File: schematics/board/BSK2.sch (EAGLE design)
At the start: 18 parts

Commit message: Реструктурированы сигналы коммутации для плат БСК
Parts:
- renumbered VAR1 to BSK1
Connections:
- net KEM1 renamed B2_KEM+
- net KEM2 renamed B2_KEM-
- net KHEAT1 renamed B2_KHEAT
- net KVCC1 renamed B2_KVCC
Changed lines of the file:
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@@
 <part name="U$11" library="CanCubeSat" deviceset="KCONNECT" device=""/>
 <part name="U$12" library="CanCubeSat" deviceset="KCONNECT" device=""/>
-<part name="VAR1" library="pinheadCS" deviceset="PINHD-1X8" device=""/>
+<part name="BSK1" library="pinheadCS" deviceset="PINHD-1X8" device=""/>
 </parts>
 <sheets>
@@
 <attribute name="NAME" x="140.462" y="102.362" size="1.27" layer="95"/>
 </instance>
-<instance part="VAR1" gate="A" x="154.94" y="175.26" smashed="yes" rot="R270">
+<instance part="BSK1" gate="A" x="154.94" y="175.26" smashed="yes" rot="R270">
 <attribute name="NAME" x="168.275" y="181.61" size="1.778" layer="95" rot="R270"/>
 <attribute name="VALUE" x="142.24" y="181.61" size="1.778" layer="96" rot="R270"/>
@@
 <wire x1="165.1" y1="177.8" x2="165.1" y2="190.5" width="0.1524" layer="91"/>
 <label x="165.1" y="182.88" size="1.778" layer="95" rot="R90"/>
-<pinref part="VAR1" gate="A" pin="1"/>
+<pinref part="BSK1" gate="A" pin="1"/>
 </segment>
 </net>
@@
 <wire x1="149.86" y1="177.8" x2="149.86" y2="190.5" width="0.1524" layer="91"/>
 <label x="149.86" y="182.88" size="1.778" layer="95" rot="R90"/>
-<pinref part="VAR1" gate="A" pin="7"/>
+<pinref part="BSK1" gate="A" pin="7"/>
 </segment>
 <segment>
@@
 <wire x1="152.4" y1="177.8" x2="152.4" y2="190.5" width="0.1524" layer="91"/>
 <label x="152.4" y="182.88" size="1.778" layer="95" rot="R90"/>
-<pinref part="VAR1" gate="A" pin="6"/>
+<pinref part="BSK1" gate="A" pin="6"/>
 </segment>
 </net>
-<net name="KEM1" class="0">
+<net name="B2_KEM+" class="0">
 <segment>
 <wire x1="160.02" y1="177.8" x2="160.02" y2="190.5" width="0.1524" layer="91"/>
 <label x="160.02" y="182.88" size="1.778" layer="95" rot="R90"/>
-<pinref part="VAR1" gate="A" pin="3"/>
+<pinref part="BSK1" gate="A" pin="3"/>
 </segment>
 <segment>
@@
 </segment>
 </net>
-<net name="KEM2" class="0">
+<net name="B2_KEM-" class="0">
 <segment>
 <wire x1="162.56" y1="177.8" x2="162.56" y2="190.5" width="0.1524" layer="91"/>
 <label x="162.56" y="182.88" size="1.778" layer="95" rot="R90"/>
-<pinref part="VAR1" gate="A" pin="2"/>
+<pinref part="BSK1" gate="A" pin="2"/>
 </segment>
 <segment>
@@
 </segment>
 </net>
-<net name="KHEAT1" class="0">
+<net name="B2_KHEAT" class="0">
 <segment>
 <wire x1="157.48" y1="177.8" x2="157.48" y2="190.5" width="0.1524" layer="91"/>
 <label x="157.48" y="182.88" size="1.778" layer="95" rot="R90"/>
-<pinref part="VAR1" gate="A" pin="4"/>
+<pinref part="BSK1" gate="A" pin="4"/>
 </segment>
 <segment>
@@
 </segment>
 </net>
-<net name="KVCC1" class="0">
+<net name="B2_KVCC" class="0">
 <segment>
 <wire x1="154.94" y1="177.8" x2="154.94" y2="190.5" width="0.1524" layer="91"/>
 <label x="154.94" y="182.88" size="1.778" layer="95" rot="R90"/>
-<pinref part="VAR1" gate="A" pin="5"/>
+<pinref part="BSK1" gate="A" pin="5"/>
 </segment>
 <segment>
@@
 <wire x1="147.32" y1="177.8" x2="147.32" y2="190.5" width="0.1524" layer="91"/>
 <label x="147.32" y="182.88" size="1.778" layer="95" rot="R90"/>
-<pinref part="VAR1" gate="A" pin="8"/>
-</segment>
-<segment>
+<pinref part="BSK1" gate="A" pin="8"/>
+</segment>
+<segment>

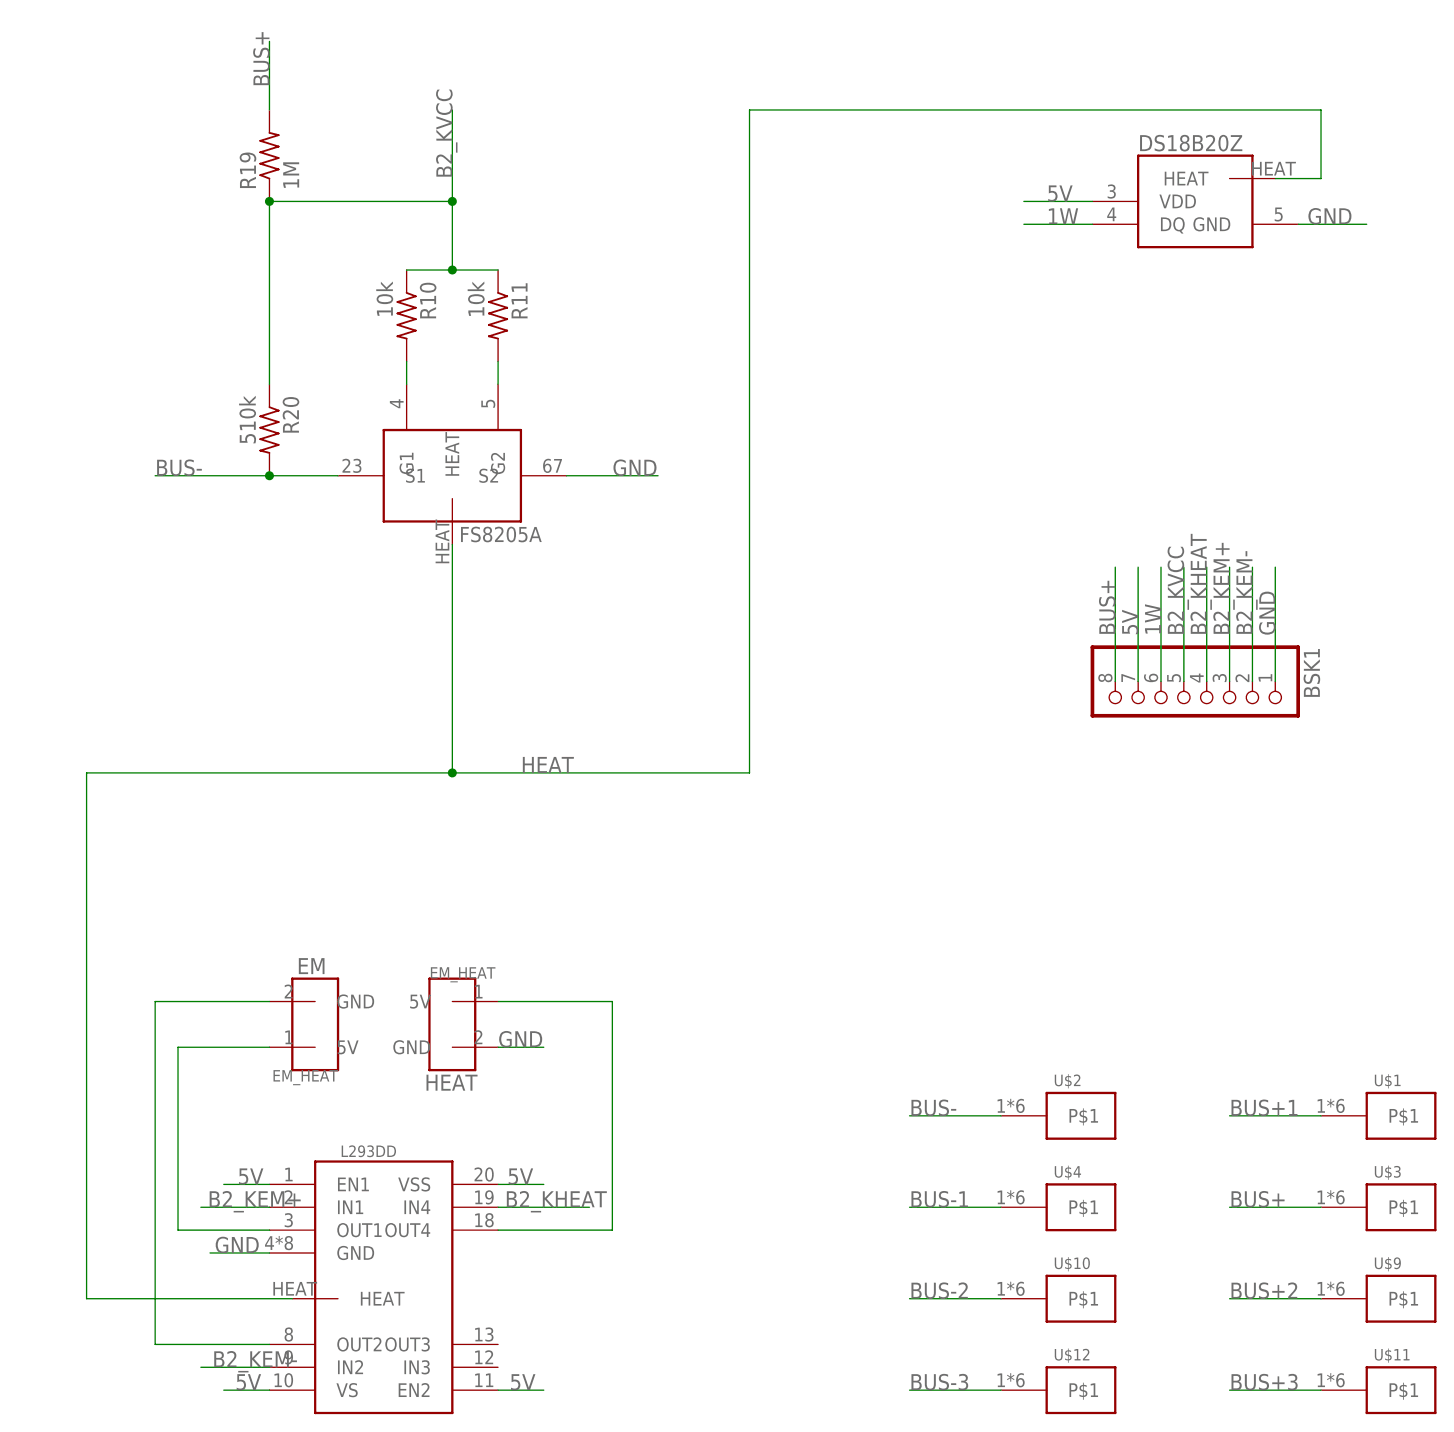
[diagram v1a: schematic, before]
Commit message: Разведены платы БСК2-5
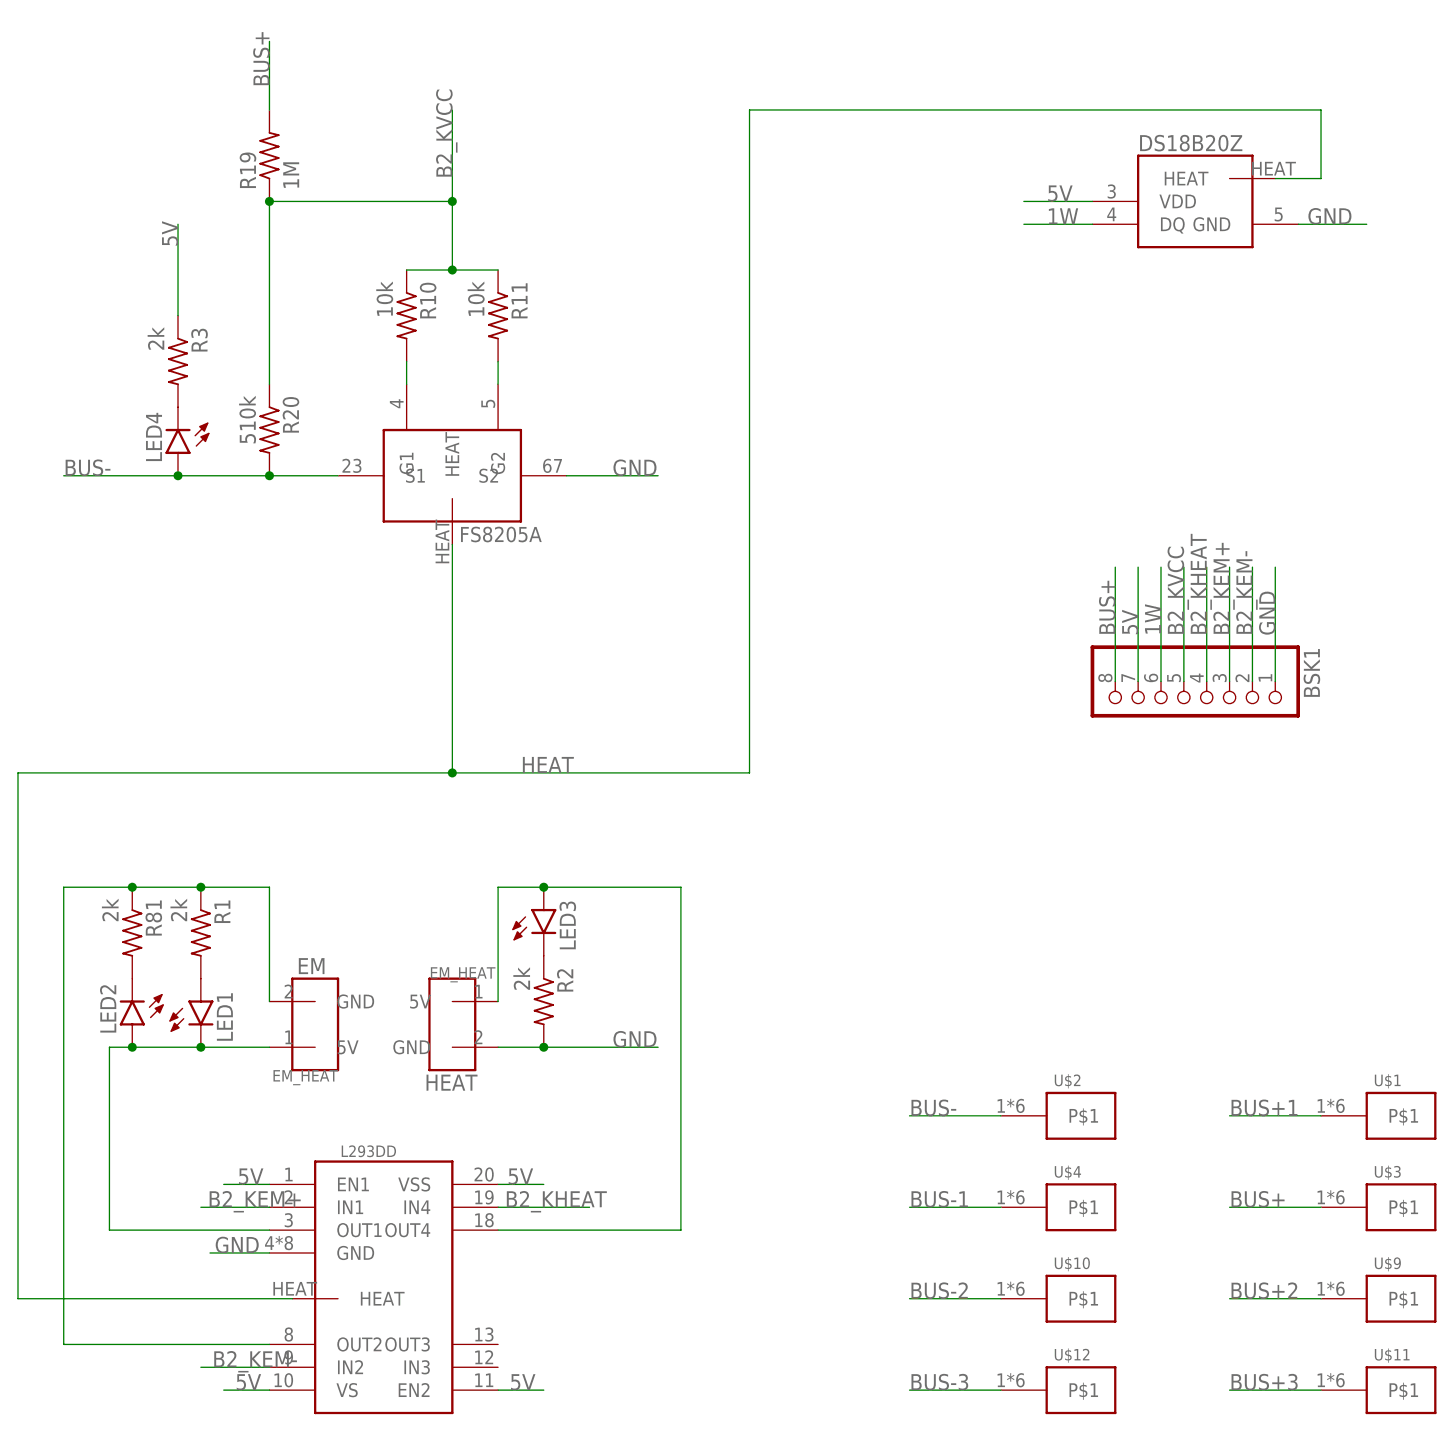
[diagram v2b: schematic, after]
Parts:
- added LED1, LED2, LED3, LED4: (no value), led:LEDCHIPLED_0603
- added R1, R2, R3, R81: 2k, resistor:R-US_R0603
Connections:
- new net N$22: LED2.C, R81.2
- new net N$23: LED1.A, R1.2
- new net N$24: LED3.C, R2.1
- new net N$25: LED4.C, R3.2
- net 5V: now also R3.1
- net BUS-: now also LED4.A
- net GND: now also R2.2
- net N$1: now also LED1.C, LED2.A
- net N$2: now also R1.1, R81.1
- net N$3: now also LED3.A
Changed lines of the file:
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@@
 <part name="U$12" library="CanCubeSat" deviceset="KCONNECT" device=""/>
 <part name="BSK1" library="pinheadCS" deviceset="PINHD-1X8" device=""/>
+<part name="LED2" library="led" library_urn="urn:adsk.eagle:library:259" deviceset="LED" device="CHIPLED_0603" package3d_urn="urn:adsk.eagle:package:15822/2"/>
+<part name="R81" library="resistor" library_urn="urn:adsk.eagle:library:348" deviceset="R-US_" device="R0603" package3d_urn="urn:adsk.eagle:package:23555/3" value="2k"/>
+<part name="R1" library="resistor" library_urn="urn:adsk.eagle:library:348" deviceset="R-US_" device="R0603" package3d_urn="urn:adsk.eagle:package:23555/3" value="2k"/>
+<part name="LED1" library="led" library_urn="urn:adsk.eagle:library:259" deviceset="LED" device="CHIPLED_0603" package3d_urn="urn:adsk.eagle:package:15822/2"/>
+<part name="R2" library="resistor" library_urn="urn:adsk.eagle:library:348" deviceset="R-US_" device="R0603" package3d_urn="urn:adsk.eagle:package:23555/3" value="2k"/>
+<part name="LED3" library="led" library_urn="urn:adsk.eagle:library:259" deviceset="LED" device="CHIPLED_0603" package3d_urn="urn:adsk.eagle:package:15822/2"/>
+<part name="LED4" library="led" library_urn="urn:adsk.eagle:library:259" deviceset="LED" device="CHIPLED_0603" package3d_urn="urn:adsk.eagle:package:15822/2"/>
+<part name="R3" library="resistor" library_urn="urn:adsk.eagle:library:348" deviceset="R-US_" device="R0603" package3d_urn="urn:adsk.eagle:package:23555/3" value="2k"/>
 </parts>
 <sheets>
@@
 <attribute name="VALUE" x="142.24" y="181.61" size="1.778" layer="96" rot="R270"/>
 </instance>
+<instance part="LED2" gate="G$1" x="38.1" y="139.7" smashed="yes" rot="R180">
+<attribute name="NAME" x="34.544" y="144.272" size="1.778" layer="95" rot="R270"/>
+<attribute name="VALUE" x="32.385" y="144.272" size="1.778" layer="96" rot="R270"/>
+</instance>
+<instance part="R81" gate="G$1" x="38.1" y="149.86" smashed="yes" rot="R270">
+<attribute name="NAME" x="39.5986" y="153.67" size="1.778" layer="95" rot="R270"/>
+<attribute name="VALUE" x="34.798" y="153.67" size="1.778" layer="96" rot="R270"/>
+</instance>
+<instance part="R1" gate="G$1" x="45.72" y="149.86" smashed="yes" rot="R270">
+<attribute name="NAME" x="47.2186" y="153.67" size="1.778" layer="95" rot="R270"/>
+<attribute name="VALUE" x="42.418" y="153.67" size="1.778" layer="96" rot="R270"/>
+</instance>
+<instance part="LED1" gate="G$1" x="45.72" y="142.24" smashed="yes">
+<attribute name="NAME" x="49.276" y="137.668" size="1.778" layer="95" rot="R90"/>
+<attribute name="VALUE" x="51.435" y="137.668" size="1.778" layer="96" rot="R90"/>
+</instance>
+<instance part="R2" gate="G$1" x="83.82" y="142.24" smashed="yes" rot="R270">
+<attribute name="NAME" x="85.3186" y="146.05" size="1.778" layer="95" rot="R270"/>
+<attribute name="VALUE" x="80.518" y="146.05" size="1.778" layer="96" rot="R270"/>
+</instance>
+<instance part="LED3" gate="G$1" x="83.82" y="152.4" smashed="yes">
+<attribute name="NAME" x="87.376" y="147.828" size="1.778" layer="95" rot="R90"/>
+<attribute name="VALUE" x="89.535" y="147.828" size="1.778" layer="96" rot="R90"/>
+</instance>
+<instance part="LED4" gate="G$1" x="43.18" y="203.2" smashed="yes" rot="R180">
+<attribute name="NAME" x="39.624" y="207.772" size="1.778" layer="95" rot="R270"/>
+<attribute name="VALUE" x="37.465" y="207.772" size="1.778" layer="96" rot="R270"/>
+</instance>
+<instance part="R3" gate="G$1" x="43.18" y="213.36" smashed="yes" rot="R270">
+<attribute name="NAME" x="44.6786" y="217.17" size="1.778" layer="95" rot="R270"/>
+<attribute name="VALUE" x="39.878" y="217.17" size="1.778" layer="96" rot="R270"/>
+</instance>
 </instances>
 <busses>
@@
 <segment>
 <wire x1="78.74" y1="137.16" x2="83.82" y2="137.16" width="0.1524" layer="91"/>
-<label x="78.74" y="137.16" size="1.778" layer="95"/>
+<label x="91.44" y="137.16" size="1.778" layer="95"/>
 <pinref part="U$7" gate="G$1" pin="GND"/>
+<pinref part="R2" gate="G$1" pin="2"/>
+<wire x1="83.82" y1="137.16" x2="96.52" y2="137.16" width="0.1524" layer="91"/>
+<junction x="83.82" y="137.16"/>
 </segment>
 <segment>
@@
 <label x="139.7" y="231.14" size="1.778" layer="95"/>
 </segment>
+<segment>
+<wire x1="43.18" y1="218.44" x2="43.18" y2="228.6" width="0.1524" layer="91"/>
+<pinref part="R3" gate="G$1" pin="1"/>
+<label x="43.18" y="226.06" size="1.778" layer="95" rot="R90"/>
+</segment>
 </net>
 <net name="1W" class="0">
@@
 <segment>
 <pinref part="U$6" gate="G$1" pin="5V"/>
-<wire x1="53.34" y1="137.16" x2="43.18" y2="137.16" width="0.1524" layer="91"/>
-<wire x1="43.18" y1="137.16" x2="43.18" y2="116.84" width="0.1524" layer="91"/>
+<wire x1="53.34" y1="137.16" x2="45.72" y2="137.16" width="0.1524" layer="91"/>
+<wire x1="45.72" y1="137.16" x2="38.1" y2="137.16" width="0.1524" layer="91"/>
+<wire x1="38.1" y1="137.16" x2="35.56" y2="137.16" width="0.1524" layer="91"/>
+<wire x1="35.56" y1="137.16" x2="35.56" y2="116.84" width="0.1524" layer="91"/>
 <pinref part="U$8" gate="G$1" pin="OUT1"/>
-<wire x1="43.18" y1="116.84" x2="53.34" y2="116.84" width="0.1524" layer="91"/>
+<wire x1="35.56" y1="116.84" x2="53.34" y2="116.84" width="0.1524" layer="91"/>
+<pinref part="LED2" gate="G$1" pin="A"/>
+<junction x="38.1" y="137.16"/>
+<pinref part="LED1" gate="G$1" pin="C"/>
+<junction x="45.72" y="137.16"/>
 </segment>
 </net>
 <net name="N$2" class="0">
 <segment>
+<wire x1="30.48" y1="154.94" x2="30.48" y2="104.14" width="0.1524" layer="91"/>
+<pinref part="U$8" gate="G$1" pin="OUT2"/>
+<wire x1="30.48" y1="104.14" x2="53.34" y2="104.14" width="0.1524" layer="91"/>
 <pinref part="U$6" gate="G$1" pin="GND"/>
-<wire x1="53.34" y1="142.24" x2="40.64" y2="142.24" width="0.1524" layer="91"/>
-<wire x1="40.64" y1="142.24" x2="40.64" y2="104.14" width="0.1524" layer="91"/>
-<pinref part="U$8" gate="G$1" pin="OUT2"/>
-<wire x1="40.64" y1="104.14" x2="53.34" y2="104.14" width="0.1524" layer="91"/>
+<wire x1="53.34" y1="142.24" x2="53.34" y2="154.94" width="0.1524" layer="91"/>
+<wire x1="53.34" y1="154.94" x2="45.72" y2="154.94" width="0.1524" layer="91"/>
+<pinref part="R81" gate="G$1" pin="1"/>
+<wire x1="45.72" y1="154.94" x2="38.1" y2="154.94" width="0.1524" layer="91"/>
+<wire x1="38.1" y1="154.94" x2="30.48" y2="154.94" width="0.1524" layer="91"/>
+<junction x="38.1" y="154.94"/>
+<pinref part="R1" gate="G$1" pin="1"/>
+<junction x="45.72" y="154.94"/>
 </segment>
 </net>
 <net name="N$3" class="0">
 <segment>
+<wire x1="99.06" y1="154.94" x2="99.06" y2="116.84" width="0.1524" layer="91"/>
+<pinref part="U$8" gate="G$1" pin="OUT4"/>
+<wire x1="99.06" y1="116.84" x2="78.74" y2="116.84" width="0.1524" layer="91"/>
 <pinref part="U$7" gate="G$1" pin="5V"/>
-<wire x1="78.74" y1="142.24" x2="91.44" y2="142.24" width="0.1524" layer="91"/>
-<wire x1="91.44" y1="142.24" x2="91.44" y2="116.84" width="0.1524" layer="91"/>
-<pinref part="U$8" gate="G$1" pin="OUT4"/>
-<wire x1="91.44" y1="116.84" x2="78.74" y2="116.84" width="0.1524" layer="91"/>
+<wire x1="78.74" y1="142.24" x2="78.74" y2="154.94" width="0.1524" layer="91"/>
+<wire x1="78.74" y1="154.94" x2="83.82" y2="154.94" width="0.1524" layer="91"/>
+<pinref part="LED3" gate="G$1" pin="A"/>
+<wire x1="83.82" y1="154.94" x2="99.06" y2="154.94" width="0.1524" layer="91"/>
+<junction x="83.82" y="154.94"/>
 </segment>
 </net>
@@
 <wire x1="53.34" y1="200.66" x2="60.96" y2="200.66" width="0.1524" layer="91"/>
 <pinref part="R20" gate="G$1" pin="2"/>
-<wire x1="53.34" y1="200.66" x2="40.64" y2="200.66" width="0.1524" layer="91"/>
+<wire x1="53.34" y1="200.66" x2="43.18" y2="200.66" width="0.1524" layer="91"/>
 <junction x="53.34" y="200.66"/>
-<label x="40.64" y="200.66" size="1.778" layer="95"/>
+<label x="30.48" y="200.66" size="1.778" layer="95"/>
+<pinref part="LED4" gate="G$1" pin="A"/>
+<wire x1="43.18" y1="200.66" x2="30.48" y2="200.66" width="0.1524" layer="91"/>
+<junction x="43.18" y="200.66"/>
 </segment>
 <segment>
@@
 <segment>
 <pinref part="U$8" gate="G$1" pin="HEAT"/>
-<wire x1="55.88" y1="109.22" x2="33.02" y2="109.22" width="0.1524" layer="91"/>
-<wire x1="33.02" y1="109.22" x2="33.02" y2="167.64" width="0.1524" layer="91"/>
-<wire x1="33.02" y1="167.64" x2="73.66" y2="167.64" width="0.1524" layer="91"/>
+<wire x1="55.88" y1="109.22" x2="25.4" y2="109.22" width="0.1524" layer="91"/>
+<wire x1="25.4" y1="109.22" x2="25.4" y2="167.64" width="0.1524" layer="91"/>
+<wire x1="25.4" y1="167.64" x2="73.66" y2="167.64" width="0.1524" layer="91"/>
 <pinref part="U$14" gate="G$1" pin="HEAT"/>
 <wire x1="73.66" y1="167.64" x2="73.66" y2="193.04" width="0.1524" layer="91"/>
@@
 </segment>
 </net>
+<net name="N$22" class="0">
+<segment>
+<pinref part="R81" gate="G$1" pin="2"/>
+<pinref part="LED2" gate="G$1" pin="C"/>
+</segment>
+</net>
+<net name="N$23" class="0">
+<segment>
+<pinref part="LED1" gate="G$1" pin="A"/>
+<pinref part="R1" gate="G$1" pin="2"/>
+</segment>
+</net>
+<net name="N$24" class="0">
+<segment>
+<pinref part="LED3" gate="G$1" pin="C"/>
+<pinref part="R2" gate="G$1" pin="1"/>
+</segment>
+</net>
+<net name="N$25" class="0">
+<segment>
+<pinref part="R3" gate="G$1" pin="2"/>
+<pinref part="LED4" gate="G$1" pin="C"/>
+</segment>
+</net>
